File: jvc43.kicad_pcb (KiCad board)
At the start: 6 copper layers, 101.6 x 50.8 mm, 172 parts, among them J201 8P8C_LED_Shielded, J301 8P8C_LED_Shielded, J401 USB_C_Receptacle_USB2.0, U201 LAN8831, U301 LAN8831, U401 LTC3622*DE, X101 25 MHz

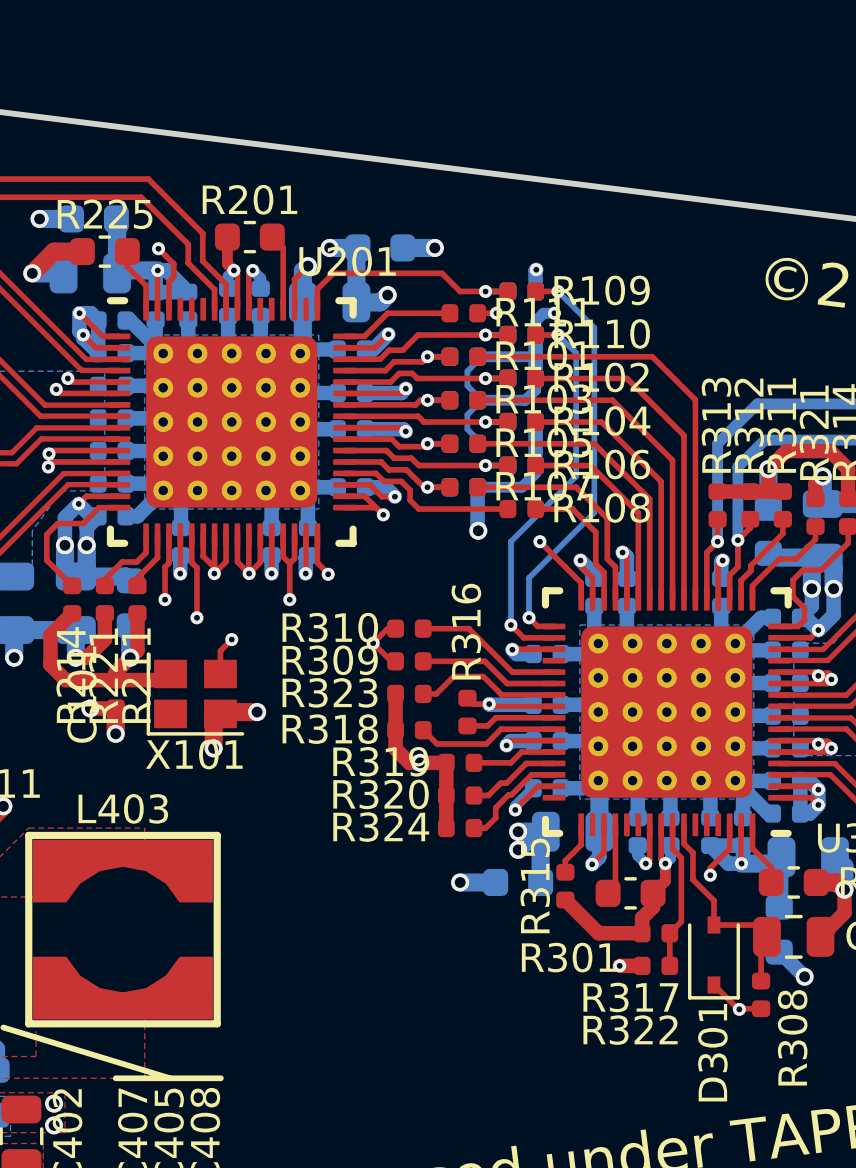
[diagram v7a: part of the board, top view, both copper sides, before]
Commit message: Eliminated one BoM line-item by caving and making the MDIO 10k resistor be size 0402 instead of 0603, to match the million other 10k 0402s.
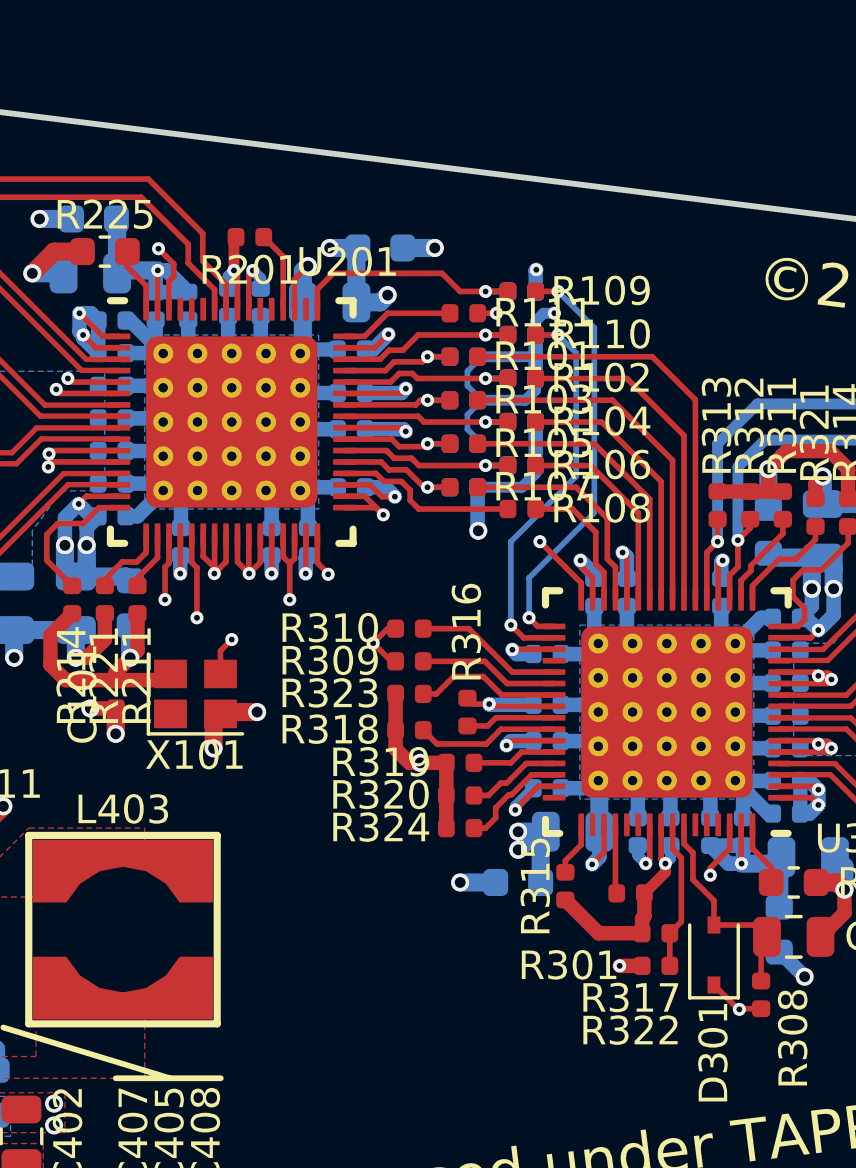
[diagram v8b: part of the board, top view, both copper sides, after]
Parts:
- R201, R301: footprint Resistor_SMD:R_0603_1608Metric -> Resistor_SMD:R_0402_1005Metric
